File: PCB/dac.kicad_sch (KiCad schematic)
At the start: 30 parts, among them X1 ASCO

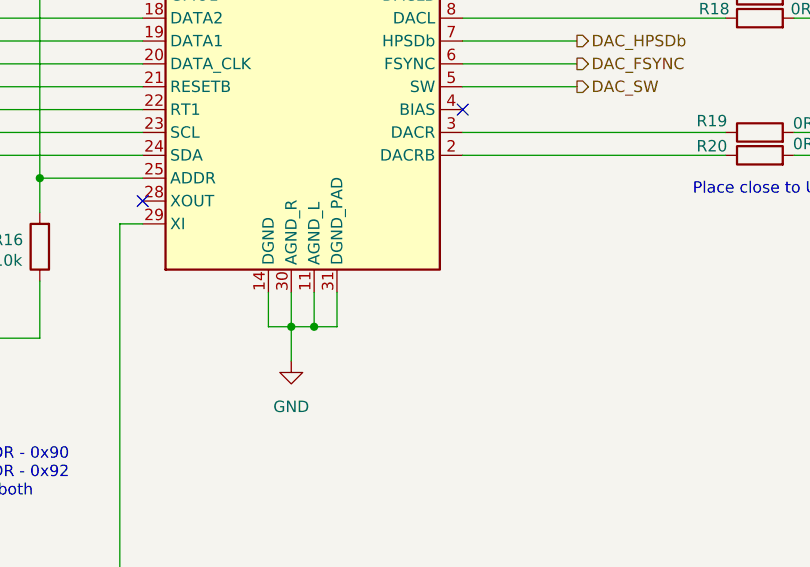
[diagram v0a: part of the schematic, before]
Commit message: Updated dac schematics and added simulations. Updated until Live 11
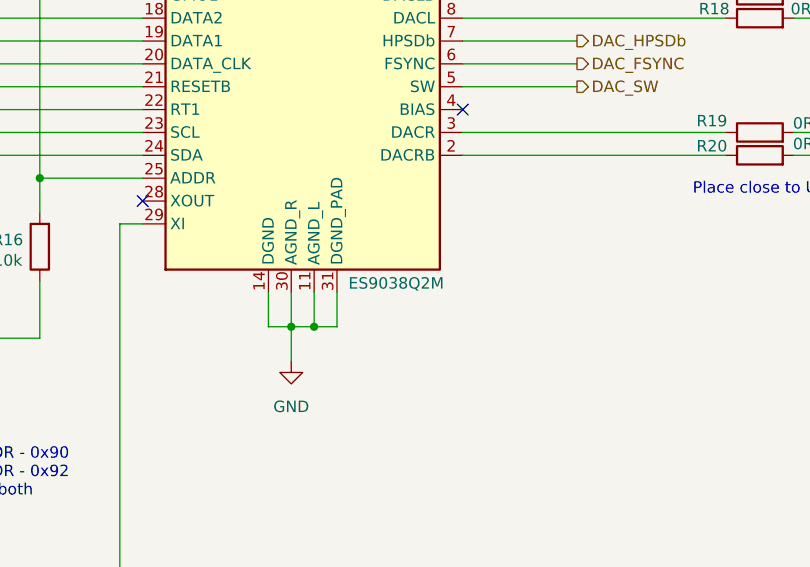
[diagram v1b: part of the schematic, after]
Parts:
- U1: value ~ -> ES9038Q2M
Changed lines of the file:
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@@
 			)
 		)
-		(property "Value" "~"
-			(at 181.2641 69.85 90)
+		(property "Value" "ES9038Q2M"
+			(at 179.07 115.824 90)
 			(effects
 				(font

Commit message: Added power supply and adjusted the AMP section to use only OPA1622 as output amp. In sync with Live 16
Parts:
- C1: footprint (none) -> Capacitor_SMD:C_0402_1005Metric_Pad0.74x0.62mm_HandSolder; Voltage 16V -> 25V
- R14: footprint (none) -> Resistor_SMD:R_0402_1005Metric_Pad0.72x0.64mm_HandSolder
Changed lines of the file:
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@@
 			)
 		)
-		(property "Footprint" ""
+		(property "Footprint" "Capacitor_SMD:C_0402_1005Metric_Pad0.74x0.62mm_HandSolder"
 			(at 107.6452 166.37 0)
 			(effects
@@
 			)
 		)
-		(property "Voltage" "16V"
+		(property "Voltage" "25V"
 			(at 106.68 162.56 0)
 			(effects
@@
 			)
 		)
-		(property "Footprint" ""
+		(property "Footprint" "Resistor_SMD:R_0402_1005Metric_Pad0.72x0.64mm_HandSolder"
 			(at 128.778 77.47 90)
 			(effects

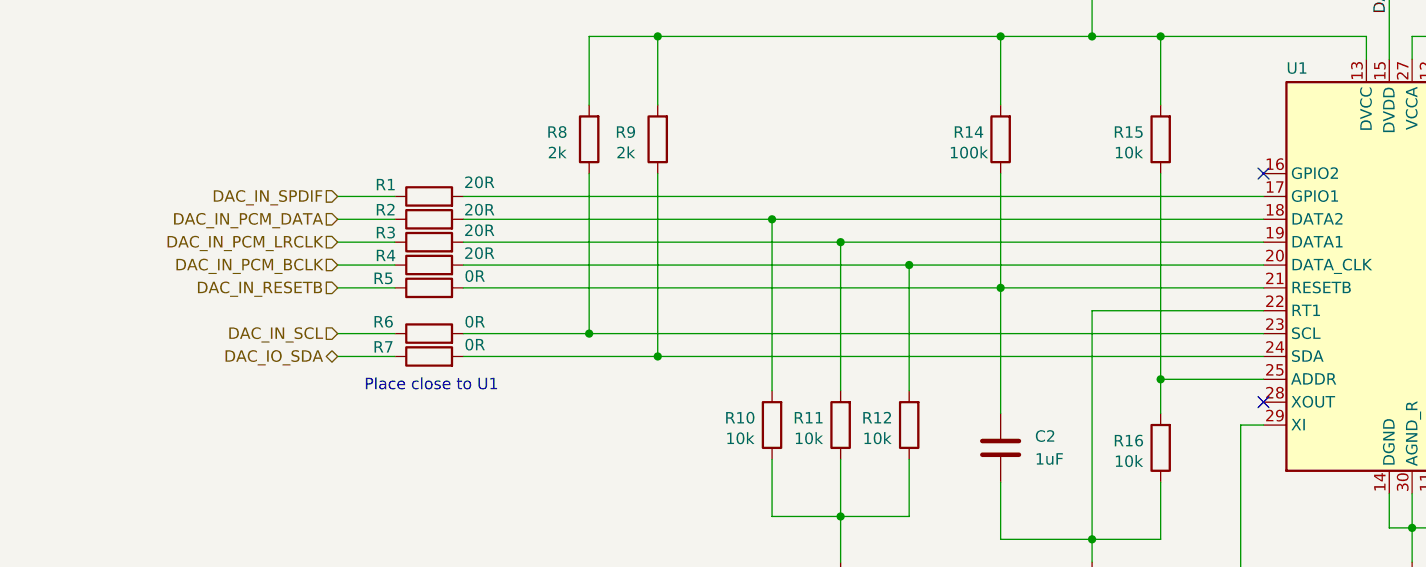
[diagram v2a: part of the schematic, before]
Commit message: Added E2P and testpoints
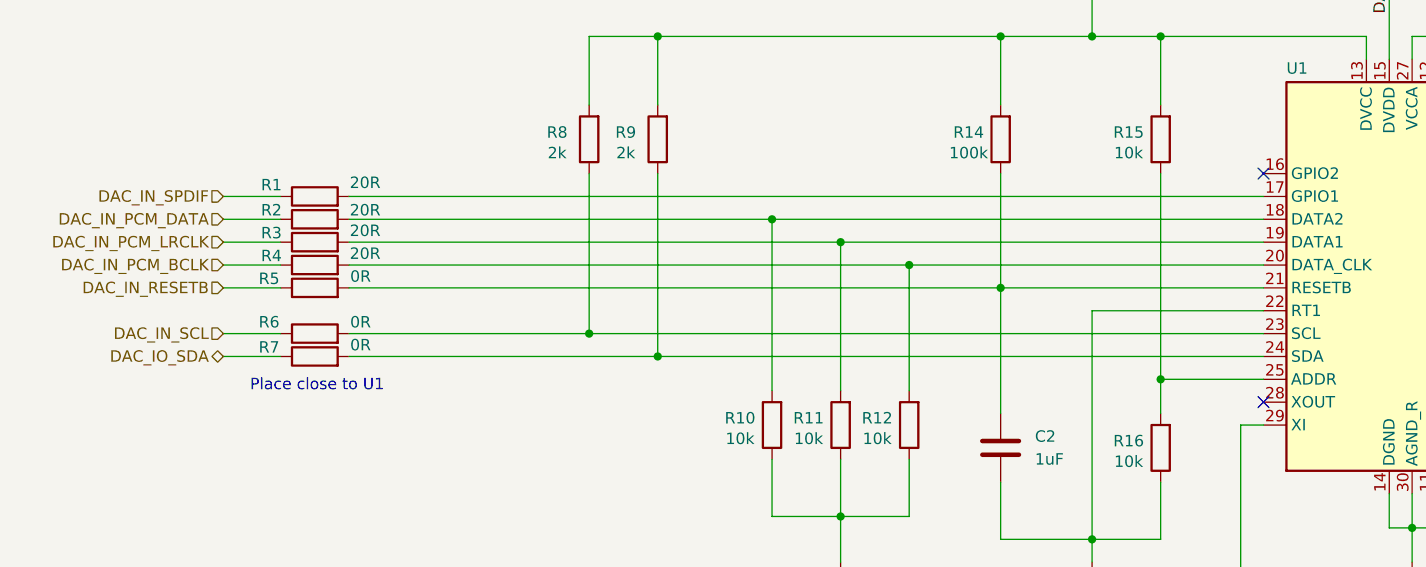
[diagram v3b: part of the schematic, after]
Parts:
- C2, C3, C4, C5, C6, C7, C8: footprint Capacitor_SMD:C_0402_1005Metric_Pad0.74x0.62mm_HandSolder -> Capacitor_SMD:C_0603_1608Metric_Pad1.08x0.95mm_HandSolder
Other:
- moved on the sheet: R1, R2, R3, R4, R5, R6, R7

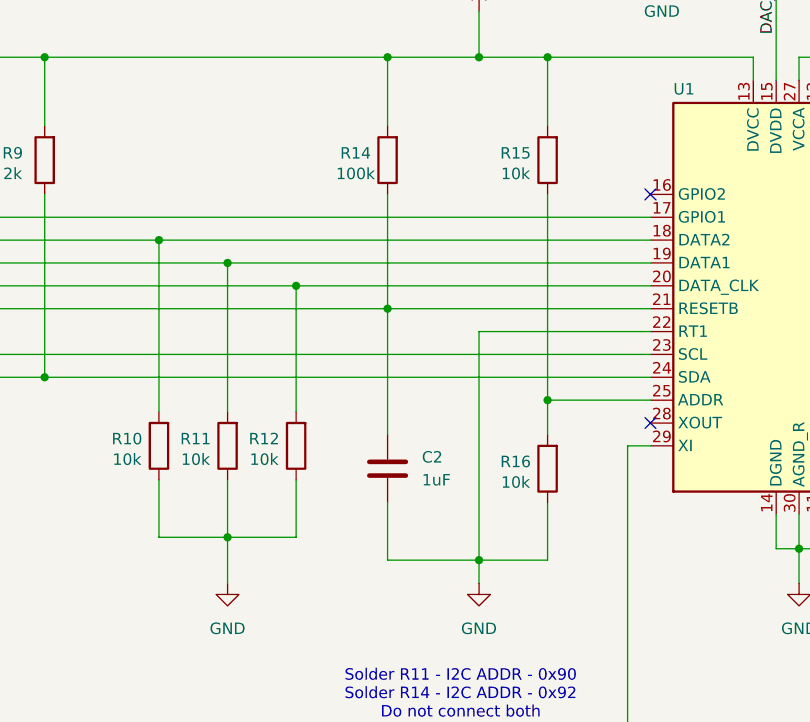
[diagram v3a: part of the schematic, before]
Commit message: Finished basic placement
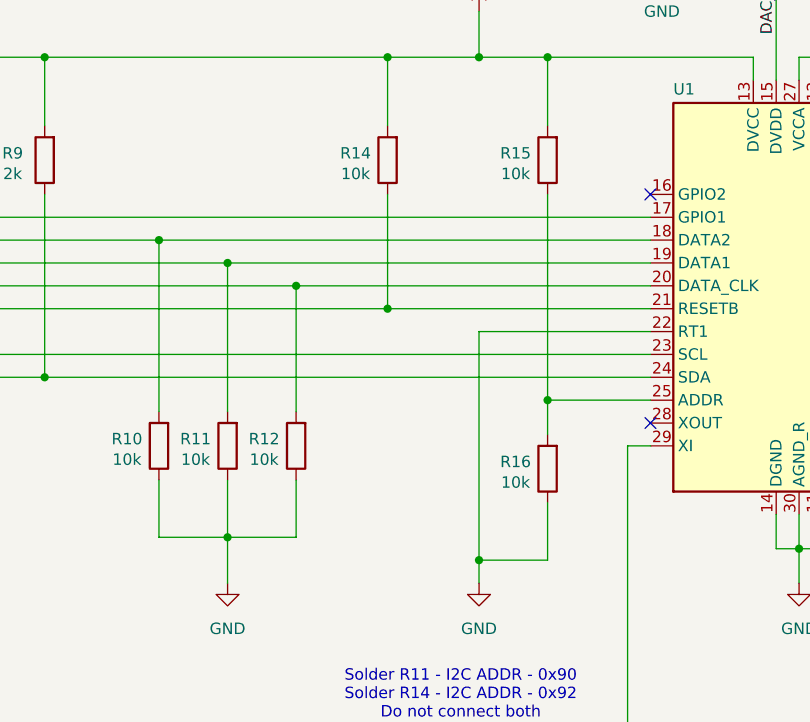
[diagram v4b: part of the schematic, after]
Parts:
- removed C2: 1uF, Capacitor_SMD:C_0603_1608Metric_Pad1.08x0.95mm_HandSolder, symbol Device:C
- R14: value 100k -> 10k
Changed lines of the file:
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@@
 	(wire
 		(pts
-			(xy 127 121.92) (xy 137.16 121.92)
-		)
-		(stroke
-			(width 0)
-			(type default)
-		)
-	)
-	(wire
-		(pts
 			(xy 109.22 119.38) (xy 116.84 119.38)
 		)
@@
 	(wire
 		(pts
-			(xy 127 93.98) (xy 127 107.95)
-		)
-		(stroke
-			(width 0)
-			(type default)
-		)
-	)
-	(wire
-		(pts
 			(xy 228.6 99.06) (xy 242.57 99.06)
 		)
@@
 	(wire
 		(pts
-			(xy 127 115.57) (xy 127 121.92)
-		)
-		(stroke
-			(width 0)
-			(type default)
-		)
-	)
-	(wire
-		(pts
 			(xy 228.6 86.36) (xy 242.57 86.36)
 		)
@@
 	)
 	(symbol
-		(lib_id "Device:C")
-		(at 127 111.76 180)
-		(unit 1)
-		(exclude_from_sim no)
-		(in_bom yes)
-		(on_board yes)
-		(dnp no)
-		(fields_autoplaced yes)
-		(property "Reference" "C2"
-			(at 130.81 110.4899 0)
-			(effects
-				(font
-					(size 1.27 1.27)
-				)
-				(justify right)
-			)
-		)
-		(property "Value" "1uF"
-			(at 130.81 113.0299 0)
-			(effects
-				(font
-					(size 1.27 1.27)
-				)
-				(justify right)
-			)
-		)
-		(property "Footprint" "Capacitor_SMD:C_0603_1608Metric_Pad1.08x0.95mm_HandSolder"
-			(at 126.0348 107.95 0)
-			(effects
-				(font
-					(size 1.27 1.27)
-				)
-				(hide yes)
-			)
-		)
-		(property "Datasheet" "~"
-			(at 127 111.76 0)
-			(effects
-				(font
-					(size 1.27 1.27)
-				)
-				(hide yes)
-			)
-		)
-		(property "Description" "Unpolarized capacitor"
-			(at 127 111.76 0)
-			(effects
-				(font
-					(size 1.27 1.27)
-				)
-				(hide yes)
-			)
-		)
-		(property "Tolerance" "10%"
-			(at 127 111.76 0)
-			(effects
-				(font
-					(size 1.27 1.27)
-				)
-				(hide yes)
-			)
-		)
-		(property "Voltage" "6.3V"
-			(at 127 111.76 0)
-			(effects
-				(font
-					(size 1.27 1.27)
-				)
-				(hide yes)
-			)
-		)
-		(pin "1"
-		)
-		(pin "2"
-		)
-		(instances
-			(project "mhd314"
-				(path "/afee45fc-2361-4efb-9cde-757fc2efd57b/e6893b8a-069a-4e5d-bc8d-bd86195d5cb0"
-					(reference "C2")
-					(unit 1)
-				)
-			)
-		)
-	)
-	(symbol
 		(lib_id "Device:R")
 		(at 144.78 77.47 180)
@@
 			)
 		)
-		(property "Value" "100k"
+		(property "Value" "10k"
 			(at 123.444 78.994 0)
 			(effects

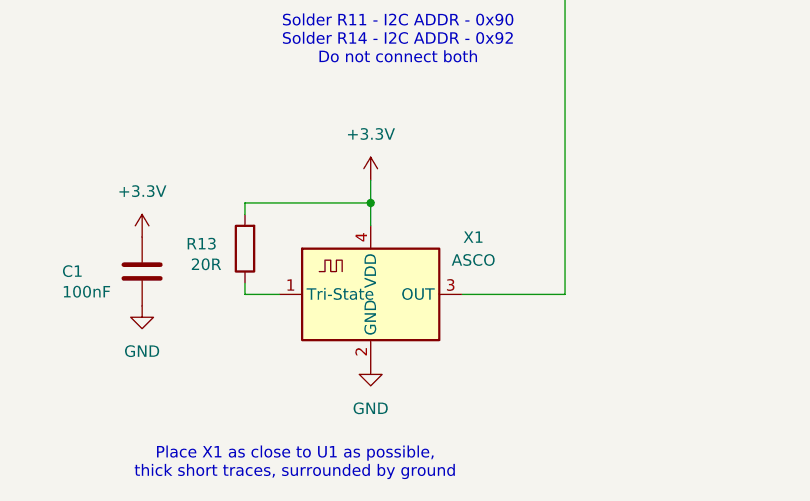
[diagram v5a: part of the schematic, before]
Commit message: Routed DAC section
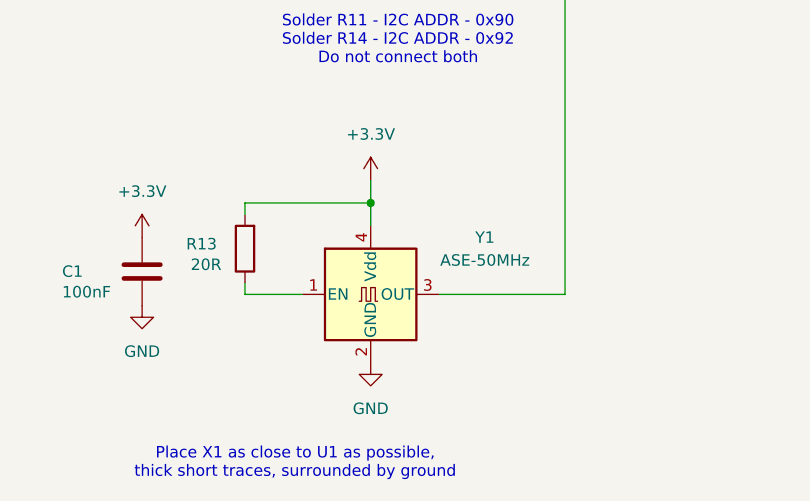
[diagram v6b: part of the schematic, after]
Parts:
- removed X1: ASCO, Oscillator:Oscillator_SMD_Abracon_ASCO-4Pin_1.6x1.2mm, symbol Oscillator:ASCO
- added Y1: ASE-50MHz, Oscillator:Oscillator_SMD_Abracon_ASE-4Pin_3.2x2.5mm, symbol Oscillator:ASE-xxxMHz
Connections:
- net +3.3V: now also Y1.4 (Vdd)
- net GND: now also Y1.2 (GND)
- net at U1.29 (XI): now also Y1.3 (OUT)
- net at R13.1: now also Y1.1 (EN)
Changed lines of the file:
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@@
 	(wire
 		(pts
+			(xy 139.7 165.1) (xy 153.67 165.1)
+		)
+		(stroke
+			(width 0)
+			(type default)
+		)
+	)
+	(wire
+		(pts
 			(xy 191.77 83.82) (xy 220.98 83.82)
 		)
@@
 	(wire
 		(pts
-			(xy 153.67 165.1) (xy 142.24 165.1)
-		)
-		(stroke
-			(width 0)
-			(type default)
-		)
-	)
-	(wire
-		(pts
 			(xy 191.77 88.9) (xy 204.47 88.9)
 		)
@@
 	(wire
 		(pts
-			(xy 118.11 165.1) (xy 121.92 165.1)
+			(xy 118.11 165.1) (xy 124.46 165.1)
 		)
 		(stroke
@@
 	)
 	(symbol
+		(lib_id "Oscillator:ASE-xxxMHz")
+		(at 132.08 165.1 0)
+		(unit 1)
+		(exclude_from_sim no)
+		(in_bom yes)
+		(on_board yes)
+		(dnp no)
+		(fields_autoplaced yes)
+		(property "Reference" "Y1"
+			(at 144.78 158.7814 0)
+			(effects
+				(font
+					(size 1.27 1.27)
+				)
+			)
+		)
+		(property "Value" "ASE-50MHz"
+			(at 144.78 161.3214 0)
+			(effects
+				(font
+					(size 1.27 1.27)
+				)
+			)
+		)
+		(property "Footprint" "Oscillator:Oscillator_SMD_Abracon_ASE-4Pin_3.2x2.5mm"
+			(at 149.86 173.99 0)
+			(effects
+				(font
+					(size 1.27 1.27)
+				)
+				(hide yes)
+			)
+		)
+		(property "Datasheet" "http://www.abracon.com/Oscillators/ASV.pdf"
+			(at 129.54 165.1 0)
+			(effects
+				(font
+					(size 1.27 1.27)
+				)
+				(hide yes)
+			)
+		)
+		(property "Description" "3.3V CMOS SMD Crystal Clock Oscillator, Abracon"
+			(at 132.08 165.1 0)
+			(effects
+				(font
+					(size 1.27 1.27)
+				)
+				(hide yes)
+			)
+		)
+		(pin "2"
+		)
+		(pin "1"
+		)
+		(pin "3"
+		)
+		(pin "4"
+		)
+		(instances
+			(project ""
+				(path "/afee45fc-2361-4efb-9cde-757fc2efd57b/e6893b8a-069a-4e5d-bc8d-bd86195d5cb0"
+					(reference "Y1")
+					(unit 1)
+				)
+			)
+		)
+	)
+	(symbol
 		(lib_id "power:+3.3VA")
 		(at 180.34 63.5 0)
@@
 					(unit 1)
 				)
-			)
-		)
-	)
-	(symbol
-		(lib_id "Oscillator:ASCO")
-		(at 132.08 165.1 0)
-		(unit 1)
-		(exclude_from_sim no)
-		(in_bom yes)
-		(on_board yes)
-		(dnp no)
-		(fields_autoplaced yes)
-		(property "Reference" "X1"
-			(at 143.51 158.7814 0)
-			(effects
-				(font
-					(size 1.27 1.27)
-				)
-			)
-		)
-		(property "Value" "ASCO"
-			(at 143.51 161.3214 0)
-			(effects
-				(font
-					(size 1.27 1.27)
-				)
-			)
-		)
-		(property "Footprint" "Oscillator:Oscillator_SMD_Abracon_ASCO-4Pin_1.6x1.2mm"
-			(at 134.62 173.99 0)
-			(effects
-				(font
-					(size 1.27 1.27)
-				)
-				(hide yes)
-			)
-		)
-		(property "Datasheet" "https://abracon.com/Oscillators/ASCO.pdf"
-			(at 126.365 161.925 0)
-			(effects
-				(font
-					(size 1.27 1.27)
-				)
-				(hide yes)
-			)
-		)
-		(property "Description" "Crystal Clock Oscillator, Abracon ASCO"
-			(at 132.08 165.1 0)
-			(effects
-				(font
-					(size 1.27 1.27)
-				)
-				(hide yes)
-			)
-		)
-		(pin "3"
-		)
-		(pin "2"
-		)
-		(pin "1"
-		)
-		(pin "4"
-		)
-		(instances
-			(project "mhd314"
-				(path "/afee45fc-2361-4efb-9cde-757fc2efd57b/e6893b8a-069a-4e5d-bc8d-bd86195d5cb0"
-					(reference "X1")
-					(unit 1)
-				)

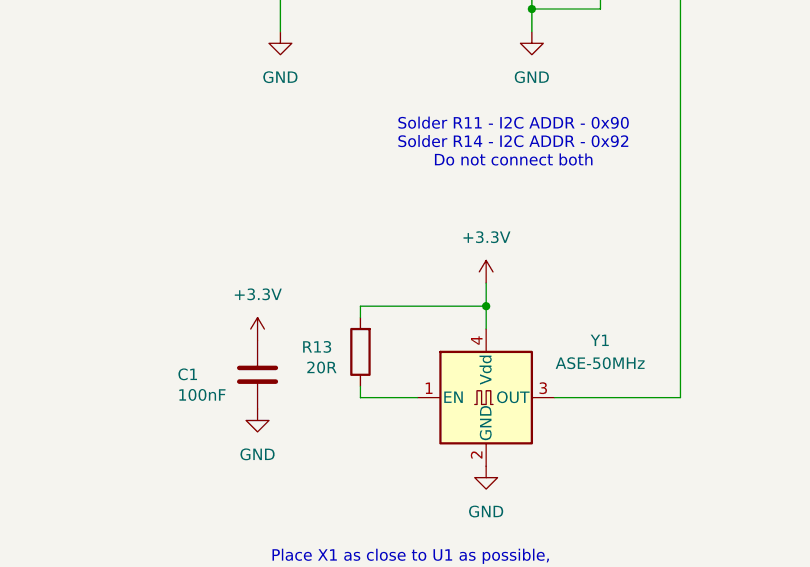
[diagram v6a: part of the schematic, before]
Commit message: Advances all basic track routing. Pending power planes, grounding and optimization
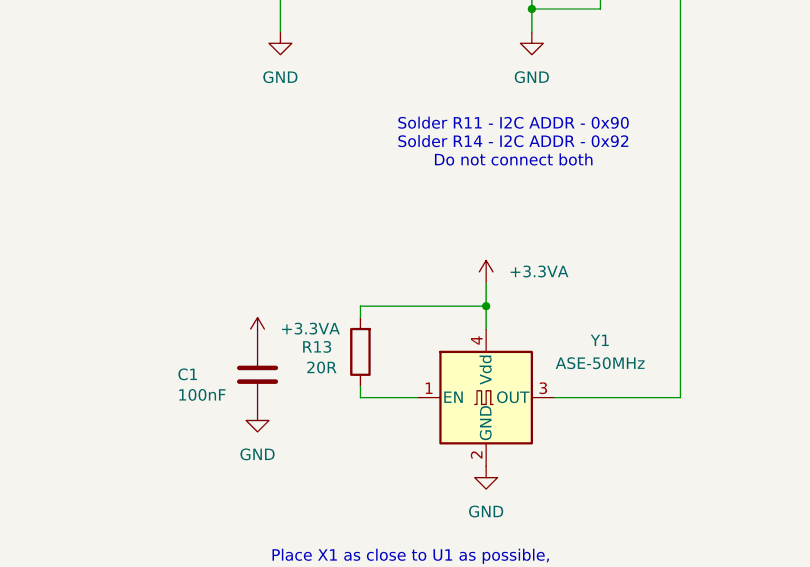
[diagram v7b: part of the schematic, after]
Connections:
- net +3.3V: no longer C1.1, R13.2, Y1.4 (Vdd)
- net +3.3VA: now also C1.1, R13.2, Y1.4 (Vdd)
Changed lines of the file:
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@@
 			)
 		)
-		(property "Value" "+3.3V"
-			(at 132.08 147.32 0)
-			(effects
-				(font
-					(size 1.27 1.27)
-				)
+		(property "Value" "+3.3VA"
+			(at 134.62 151.1299 0)
+			(effects
+				(font
+					(size 1.27 1.27)
+				)
+				(justify left)
 			)
 		)
@@
 			)
 		)
-		(property "Value" "+3.3V"
-			(at 106.68 153.67 0)
-			(effects
-				(font
-					(size 1.27 1.27)
-				)
-			)
-		)
+		(property "Value" "+3.3VA"
+			(at 109.22 157.4799 0)
+			(effects
+				(font
+					(size 1.27 1.27)
+				)
+				(justify left)
+			)
+		)

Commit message: Basic routing finished. Still missing some optimizing steps and DRC
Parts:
- U1: footprint _mahaudio KiCad Library:QFN-30_EP_3x5_Pitch0.4mm -> mahaudio KiCad Library:QFN-30_EP_3x5_Pitch0.4mm; symbol mahaudio_kicad_lib:ES9038Q2M -> mahaudio KiCad Library:ES9038Q2M
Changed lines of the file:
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@@
 	)
 	(symbol
-		(lib_id "mahaudio_kicad_lib:ES9038Q2M")
+		(lib_id "mahaudio KiCad Library:ES9038Q2M")
 		(at 173.99 92.71 90)
 		(unit 1)
@@
 			)
 		)
-		(property "Footprint" "_mahaudio KiCad Library:QFN-30_EP_3x5_Pitch0.4mm"
+		(property "Footprint" "mahaudio KiCad Library:QFN-30_EP_3x5_Pitch0.4mm"
 			(at 170.18 71.12 0)
 			(effects
